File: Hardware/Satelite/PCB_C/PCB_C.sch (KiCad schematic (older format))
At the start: 54 parts, among them IC1 MCP1501T-33E_CHY, IC3 BQ24392RSER, J1 Conn_01x06, J3 Conector_PCB_B-C, J4 Conector_Expansion_CanSat, J5 USB_B_Micro, J6 Conn_02x03_Counter_Clockwise, M1 Spacer, M2 Spacer, M3 Spacer, U1 NTB0104BQ,115, U2 TCA9802DGKR, U3 ESP32-WROOM-32, U4 NTB0104BQ,115, U7 PIC16LF18325-ISL, Y1 LFXTAL016178

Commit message: Agregadas librerías a PCB_C y renombrados pines no usado en el conector B-C
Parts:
- removed U3: ESP32-WROOM-32, RF_Module:ESP32-WROOM-32, symbol PCB_C-rescue:ESP32-WROOM-32-RF_Module
- added U?: ESP32-WROOM-32, RF_Module:ESP32-WROOM-32, symbol RF_Module:ESP32-WROOM-32
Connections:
- net labels removed: ISET
- wire segments 305 -> 303
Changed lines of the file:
@@
 EESchema Schematic File Version 4
 LIBS:PCB_C-cache
-EELAYER 26 0
+EELAYER 29 0
 EELAYER END
 $Descr A3 16535 11693
@@
 Text Label 15100 2200 0    50   ~ 0
 GPOUT
-Text Label 15100 1700 0    50   ~ 0
-ISET
 Text Label 15100 1800 0    50   ~ 0
 CHG
@@
 Wire Wire Line
 	15000 2100 15400 2100
-Wire Wire Line
-	15000 1700 15400 1700
 Wire Wire Line
 	15000 1800 15400 1800
@@
 Text Label 5400 1950 0    50   ~ 0
 CHG
-Text Label 7900 2150 2    50   ~ 0
-ISET
 Text Label 7900 2250 2    50   ~ 0
 SDO
@@
 	10250 2200 10250 2300
 Connection ~ 10100 2200
-Wire Wire Line
-	7250 2150 7900 2150
 $Comp
 L power:GND #PWR047
@@
 Wire Wire Line
 	8150 7350 7750 7350
-$Comp
-L PCB_C-rescue:ESP32-WROOM-32-RF_Module U3
-U 1 1 5D74DFF0
-P 6650 2850
-F 0 "U3" H 5900 4350 50  0000 C CNN
-F 1 "ESP32-WROOM-32" H 6200 4250 50  0000 C CNN
-F 2 "RF_Module:ESP32-WROOM-32" H 6650 1350 50  0001 C CNN
-F 3 "https://www.espressif.com/sites/default/files/documentation/esp32-wroom-32_datasheet_en.pdf" H 6350 2900 50  0001 C CNN
-F 4 "ESP32-WROOM-32" H 6650 2850 50  0001 C CNN "Manufacturer Part Number"
-	1    6650 2850
-	1    0    0    -1
-$EndComp
 $Comp
 L power:GND #PWR017
@@
 EndData
 $EndBitmap
+$Comp
+L RF_Module:ESP32-WROOM-32 U?
+U 1 1 5D11D3F2
+P 6650 2850
+F 0 "U?" H 7050 4350 50  0000 C CNN
+F 1 "ESP32-WROOM-32" H 7050 4250 50  0000 C CNN
+F 2 "RF_Module:ESP32-WROOM-32" H 6650 1350 50  0001 C CNN
+F 3 "https://www.espressif.com/sites/default/files/documentation/esp32-wroom-32_datasheet_en.pdf" H 6350 2900 50  0001 C CNN
+	1    6650 2850
+	1    0    0    -1
+$EndComp
 $EndSCHEMATC

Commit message: Eliminado circuito de detección de cargador de PCB_C, siempre usamos toda la corriente de carga ahora.
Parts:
- removed IC3: BQ24392RSER, SamacSys_Parts:RSE(R-PUQFN-N10), symbol SamacSys_Parts:BQ24392RSER
- removed R8: 5k6, Resistor_SMD:R_0603_1608Metric_Pad1.05x0.95mm_HandSolder, symbol Device:R
- removed R9: 10k, Resistor_SMD:R_0603_1608Metric_Pad1.05x0.95mm_HandSolder, symbol Device:R
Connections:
- wire segments 303 -> 286
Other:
- note added: "USB"
- note removed: "USB y detección de cargador"
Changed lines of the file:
@@
 $EndComp
-Wire Wire Line
-	15350 9100 14800 9100
-Wire Wire Line
-	14800 9000 15350 9000
 Wire Wire Line
 	15650 9400 15650 9450
@@
 Wire Wire Line
 	15750 9450 15700 9450
-$Comp
-L SamacSys_Parts:BQ24392RSER IC3
-U 1 1 5BBE8A84
-P 13300 8800
-F 0 "IC3" H 14050 9065 50  0000 C CNN
-F 1 "BQ24392RSER" H 14050 8974 50  0000 C CNN
-F 2 "SamacSys_Parts:RSE(R-PUQFN-N10)" H 14650 8900 50  0001 L CNN
-F 3 "http://www.ti.com/lit/gpn/bq24392" H 14650 8800 50  0001 L CNN
-F 4 "SPST USB 2.0 High-Speed Switch With Battery Charging Detection" H 14650 8700 50  0001 L CNN "Description"
-F 5 "Texas Instruments" H 14650 8500 50  0001 L CNN "Manufacturer_Name"
-F 6 "BQ24392RSER" H 14650 8400 50  0001 L CNN "Manufacturer Part Number"
-F 7 "8279327P" H 14650 8300 50  0001 L CNN "RS Part Number"
-F 8 "http://uk.rs-online.com/web/p/products/8279327P" H 14650 8200 50  0001 L CNN "RS Price/Stock"
-F 9 "BQ24392RSER" H 14650 8100 50  0001 L CNN "Arrow Part Number"
-F 10 "https://www.arrow.com/en/products/bq24392rser/texas-instruments" H 14650 8000 50  0001 L CNN "Arrow Price/Stock"
-	1    13300 8800
-	1    0    0    -1
-$EndComp
-Wire Wire Line
-	14800 8800 15050 8800
 Wire Wire Line
 	15050 8750 15050 8800
-Connection ~ 15050 8800
 Wire Wire Line
 	15050 8800 15350 8800
-$Comp
-L power:GND #PWR058
-U 1 1 5BBEBEBA
-P 14950 9500
-F 0 "#PWR058" H 14950 9250 50  0001 C CNN
-F 1 "GND" H 14955 9327 50  0000 C CNN
-F 2 "" H 14950 9500 50  0001 C CNN
-F 3 "" H 14950 9500 50  0001 C CNN
-	1    14950 9500
-	1    0    0    -1
-$EndComp
-Wire Wire Line
-	14800 9300 14950 9300
-Wire Wire Line
-	14950 9300 14950 9500
-Text Label 11900 9050 0    50   ~ 0
-CHG_DETECT
-$Comp
-L power:VBUS #PWR045
-U 1 1 5BC0A264
-P 13050 9250
-F 0 "#PWR045" H 13050 9100 50  0001 C CNN
-F 1 "VBUS" H 13065 9423 50  0000 C CNN
-F 2 "" H 13050 9250 50  0001 C CNN
-F 3 "" H 13050 9250 50  0001 C CNN
-	1    13050 9250
-	1    0    0    -1
-$EndComp
-Wire Notes Line
-	11800 8100 16000 8100
+Wire Notes Line
+	14850 8100 16000 8100
 Wire Notes Line
 	16000 8100 16000 9800
 Wire Notes Line
-	16000 9800 11800 9800
-Wire Notes Line
-	11800 9800 11800 8100
-Text Notes 12550 8350 0    118  ~ 0
-USB y detección de cargador
+	16000 9800 14850 9800
+Wire Notes Line
+	14850 9800 14850 8100
+Text Notes 15200 8350 0    118  ~ 0
+USB
 Wire Notes Line
 	550  3050 3550 3050
@@
 Text Label 5250 5800 0    50   ~ 0
 I_SENSE_BATT
-Text Label 5400 1850 0    50   ~ 0
-CHG_DETECT
 Text Label 7900 2050 2    50   ~ 0
 AUX_ENABLE
@@
 	5900 5800 5250 5800
 Wire Wire Line
-	5400 1850 6050 1850
-Wire Wire Line
 	7900 3250 7250 3250
 Wire Wire Line
@@
 	15100 4650 15550 4650
 $Comp
-L Device:R R8
-U 1 1 5C2BF325
-P 12600 8850
-F 0 "R8" H 12670 8896 50  0000 L CNN
-F 1 "5k6" H 12670 8804 50  0000 L CNN
-F 2 "Resistor_SMD:R_0603_1608Metric_Pad1.05x0.95mm_HandSolder" V 12530 8850 50  0001 C CNN
-F 3 "~" H 12600 8850 50  0001 C CNN
-F 4 "RC0603FR-075K6L" H 12600 8850 50  0001 C CNN "Manufacturer Part Number"
-	1    12600 8850
-	1    0    0    -1
-$EndComp
-Wire Wire Line
-	13050 9250 13250 9250
-Wire Wire Line
-	13250 9250 13250 9200
-Wire Wire Line
-	13250 9200 13300 9200
-$Comp
-L Device:R R9
-U 1 1 5C3B0D3B
-P 12600 9250
-F 0 "R9" H 12670 9296 50  0000 L CNN
-F 1 "10k" H 12670 9204 50  0000 L CNN
-F 2 "Resistor_SMD:R_0603_1608Metric_Pad1.05x0.95mm_HandSolder" V 12530 9250 50  0001 C CNN
-F 3 "~" H 12600 9250 50  0001 C CNN
-F 4 "RC0603JR-0710KL" H 12600 9250 50  0001 C CNN "Manufacturer Part Number"
-	1    12600 9250
-	1    0    0    -1
-$EndComp
-Wire Wire Line
-	13300 9000 13050 9000
-Wire Wire Line
-	13050 9000 13050 8650
-Wire Wire Line
-	13050 8650 12600 8650
-$Comp
-L power:GND #PWR011
-U 1 1 5C412A14
-P 12600 9500
-F 0 "#PWR011" H 12600 9250 50  0001 C CNN
-F 1 "GND" H 12605 9327 50  0000 C CNN
-F 2 "" H 12600 9500 50  0001 C CNN
-F 3 "" H 12600 9500 50  0001 C CNN
-	1    12600 9500
-	1    0    0    -1
-$EndComp
-Wire Wire Line
-	12600 9400 12600 9500
-Wire Wire Line
-	12600 9000 12600 9050
-Wire Wire Line
-	12600 8650 12600 8700
-Wire Wire Line
-	12600 9100 12600 9050
-Connection ~ 12600 9050
-$Comp
 L power:+BATT #PWR01
 U 1 1 5BC3E6F0
@@
 	-1   0    0    -1
 $EndComp
-Wire Wire Line
-	11900 9050 12600 9050
 $Comp
 L Graphic:Logo_Open_Hardware_Large #LOGO1

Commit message: Nuevo conector entre PCB_B y PCB_C, más fácil de soldar y robusto
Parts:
- J3: Manufacturer Part Number 10132797-025100LF -> 53307-2071; Notes Hecho con dos 10132797-025100LF y sus dos opuestos 10132798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 -> Hecho con dos 53307-2071 y sus dos opuestos 52465-2071
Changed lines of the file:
@@
 F 2 "AXTEC:Conector_PCB_B-C_Lado_C" H 14150 2200 50  0001 C CNN
 F 3 "" H 14150 2200 50  0001 C CNN
-F 4 "Hecho con dos 10132797-025100LF y sus dos opuestos 10132798-022100LF" H 0   -150 50  0001 C CNN "Notes"
-F 5 "10132797-025100LF" H 14250 1450 50  0001 C CNN "Manufacturer Part Number"
+F 4 "Hecho con dos 53307-2071 y sus dos opuestos 52465-2071" H 0   -150 50  0001 C CNN "Notes"
+F 5 "53307-2071" H 14250 1450 50  0001 C CNN "Manufacturer Part Number"
 F 6 "2" H 14250 1450 50  0001 C CNN "Quantity"
 	1    14250 1450

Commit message: ESP32 tamaño compacto sin antena PCB
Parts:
- removed U?: ESP32-WROOM-32, RF_Module:ESP32-WROOM-32, symbol RF_Module:ESP32-WROOM-32
- added U?: ESP32-WROOM-32U, RF_Module:ESP32-WROOM-32U, symbol RF_Module:ESP32-WROOM-32U
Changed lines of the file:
@@
 $EndBitmap
 $Comp
-L RF_Module:ESP32-WROOM-32 U?
-U 1 1 5D11D3F2
+L RF_Module:ESP32-WROOM-32U U?
+U 1 1 5CCE43C3
 P 6650 2850
 F 0 "U?" H 7050 4350 50  0000 C CNN
-F 1 "ESP32-WROOM-32" H 7050 4250 50  0000 C CNN
-F 2 "RF_Module:ESP32-WROOM-32" H 6650 1350 50  0001 C CNN
-F 3 "https://www.espressif.com/sites/default/files/documentation/esp32-wroom-32_datasheet_en.pdf" H 6350 2900 50  0001 C CNN
+F 1 "ESP32-WROOM-32U" H 7050 4250 50  0000 C CNN
+F 2 "RF_Module:ESP32-WROOM-32U" H 6650 1350 50  0001 C CNN
+F 3 "https://www.espressif.com/sites/default/files/documentation/esp32-wroom-32d_esp32-wroom-32u_datasheet_en.pdf" H 6350 2900 50  0001 C CNN
+F 4 "ESP32-WROOM-32U" H 6650 2850 50  0001 C CNN "Manufacturer Part Number"
 	1    6650 2850
 	1    0    0    -1

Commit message: Agregado conversor USB-Serie en PCB_C para poder programar el ESP32 desde USB
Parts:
- removed J1: Conn_01x06, Connector_PinHeader_2.54mm:PinHeader_1x06_P2.54mm_Vertical, symbol Connector_Generic:Conn_01x06
- removed JP1: BOM_Jumper, AXTEC:Empty_Footprint, symbol AXTEC_IC:BOM_Jumper
- removed L1: Inductor, Inductor_SMD:L_0805_2012Metric_Pad1.15x1.40mm_HandSolder, symbol Device:L_Core_Iron
- added C10: 100nF, Capacitor_SMD:C_0402_1005Metric, symbol Device:C_Small
- added C6: 4.7uF, Capacitor_SMD:C_0805_2012Metric_Pad1.15x1.40mm_HandSolder, symbol Device:C_Small
- added C7, C8: 47pF, Capacitor_SMD:C_0402_1005Metric, symbol Device:C_Small
- added JP1: Jumper_2_Bridged, Jumper:SolderJumper-2_P1.3mm_Bridged_Pad1.0x1.5mm, symbol Jumper:Jumper_2_Bridged
- added R8: 27R, Resistor_SMD:R_0603_1608Metric_Pad1.05x0.95mm_HandSolder, symbol Device:R
- added R9: 100k, Resistor_SMD:R_0603_1608Metric_Pad1.05x0.95mm_HandSolder, symbol Device:R
- added U3: FT231XQ, Package_DFN_QFN:QFN-20-1EP_4x4mm_P0.5mm_EP2.5x2.5mm, symbol Interface_USB:FT231XQ
- R6: value 100k -> 27R; Manufacturer Part Number RC0603JR-07100KL -> RC0603FR-0727RL
- gave numbers to parts that had none: 1
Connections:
- net labels added: D+, D-
- wire segments 286 -> 301
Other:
- note removed: "Header programación"
- moved on the sheet: C1, C13, C16, IC1, J5, M1, M2, M3, MH1, R7, TP1, TP10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

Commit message: Cambio de MCU de ESP32 a nRF52840
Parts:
- removed C13, C16: 1uF, Capacitor_SMD:C_0402_1005Metric, symbol Device:C_Small
- removed J6: Conn_02x03_Counter_Clockwise, Connector_PinHeader_1.27mm:PinHeader_2x03_P1.27mm_Vertical_SMD, symbol Connector_Generic:Conn_02x03_Counter_Clockwise
- removed JP1: Jumper_2_Bridged, Jumper:SolderJumper-2_P1.3mm_Bridged_Pad1.0x1.5mm, symbol Jumper:Jumper_2_Bridged
- removed R2, R3: 10k, Resistor_SMD:R_0603_1608Metric_Pad1.05x0.95mm_HandSolder, symbol Device:R
- removed R5, R7, R9: 100k, Resistor_SMD:R_0603_1608Metric_Pad1.05x0.95mm_HandSolder, symbol Device:R
- removed U3: FT231XQ, Package_DFN_QFN:QFN-20-1EP_4x4mm_P0.5mm_EP2.5x2.5mm, symbol Interface_USB:FT231XQ
- removed U5: ESP32-WROOM-32U, RF_Module:ESP32-WROOM-32U, symbol RF_Module:ESP32-WROOM-32U
- removed U7: PIC16LF18325-ISL, Package_SO:SOIC-14_3.9x8.7mm_P1.27mm, symbol MCU_Microchip_PIC16:PIC16LF18325-ISL
- added U3: W25Q32JVSSIQ, Package_SO:SOIC-8_3.9x4.9mm_P1.27mm, symbol SamacSys_Parts:W25Q32BVSSIG
- added U5: BL654, SamacSys_Parts:45100001, symbol AXTEC_IC:BL654
- C10: value 100nF -> 1uF; Manufacturer Part Number GCM155R71C104KA55D -> GRM155R61E105KA12D
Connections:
- net labels added: EXT_IO2, EXT_IO3, MCLK, MCS, MMISO, MMOSI, SWCLK, SWDIO, SWO, nRST
- net labels removed: EN, GPIO0, ICSDAT, ICSPCLK, MCLR
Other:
- note added: "SLOW"
- moved on the sheet: C3, C4, C6, C7, C8, J5, R1, R4, R6, R8, Y1

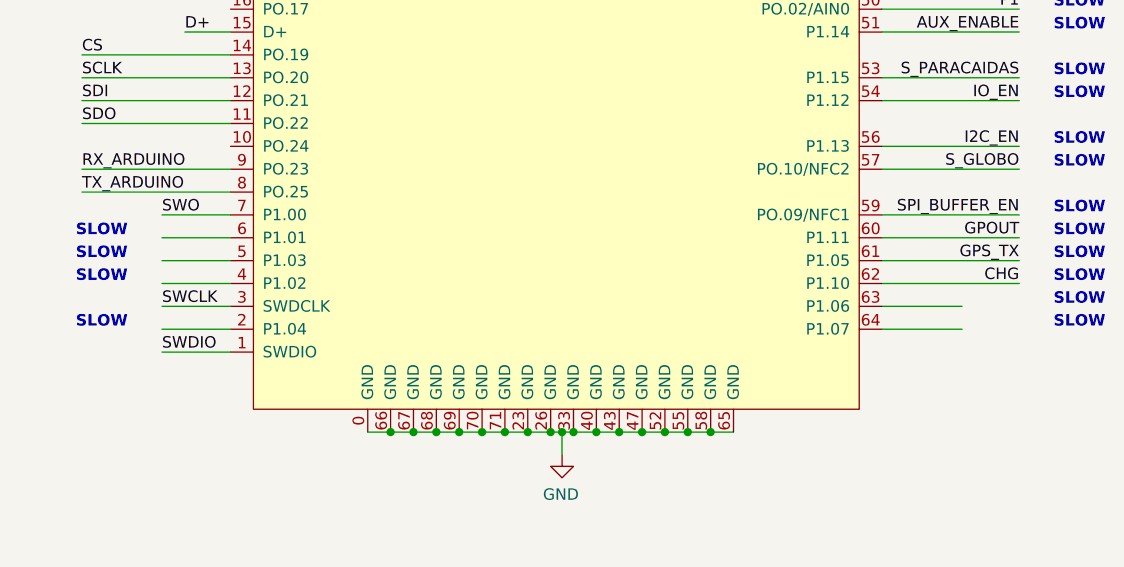
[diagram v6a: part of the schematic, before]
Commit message: Eliminación de wires no usadas en esquema de PCB_C
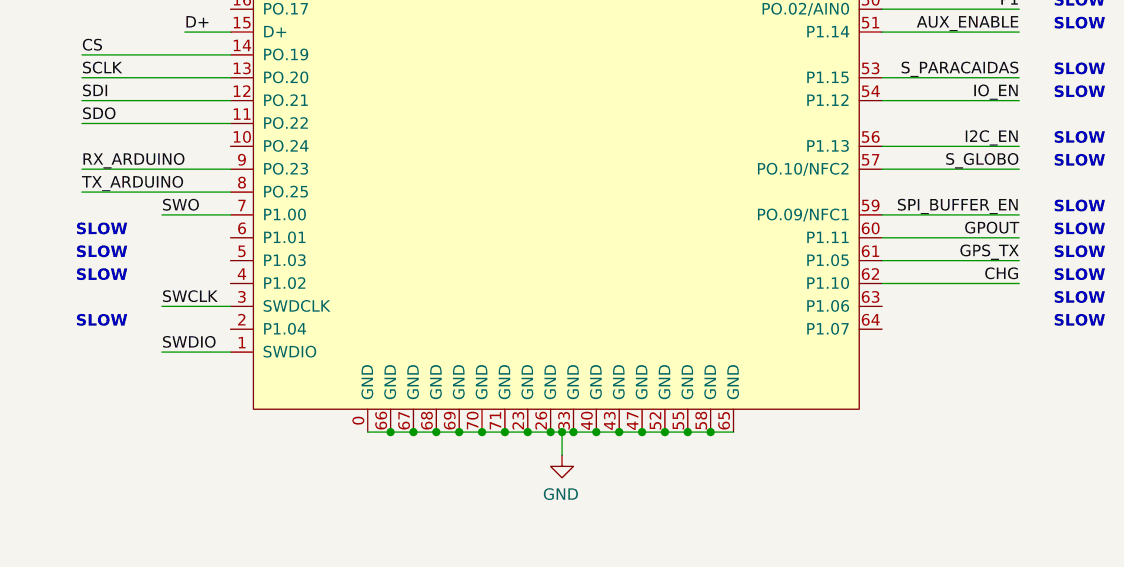
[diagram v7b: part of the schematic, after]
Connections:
- wire segments 301 -> 295
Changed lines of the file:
@@
 	9650 5050 10250 5050
 Wire Wire Line
-	9650 5550 10000 5550
-Wire Wire Line
-	9650 5450 10000 5450
-Wire Wire Line
 	9650 5250 10250 5250
-Wire Wire Line
-	6800 5550 6500 5550
-Wire Wire Line
-	6800 5350 6500 5350
-Wire Wire Line
-	6500 5250 6800 5250
-Wire Wire Line
-	6800 5150 6500 5150
 $Comp
 L power:GND #PWR015

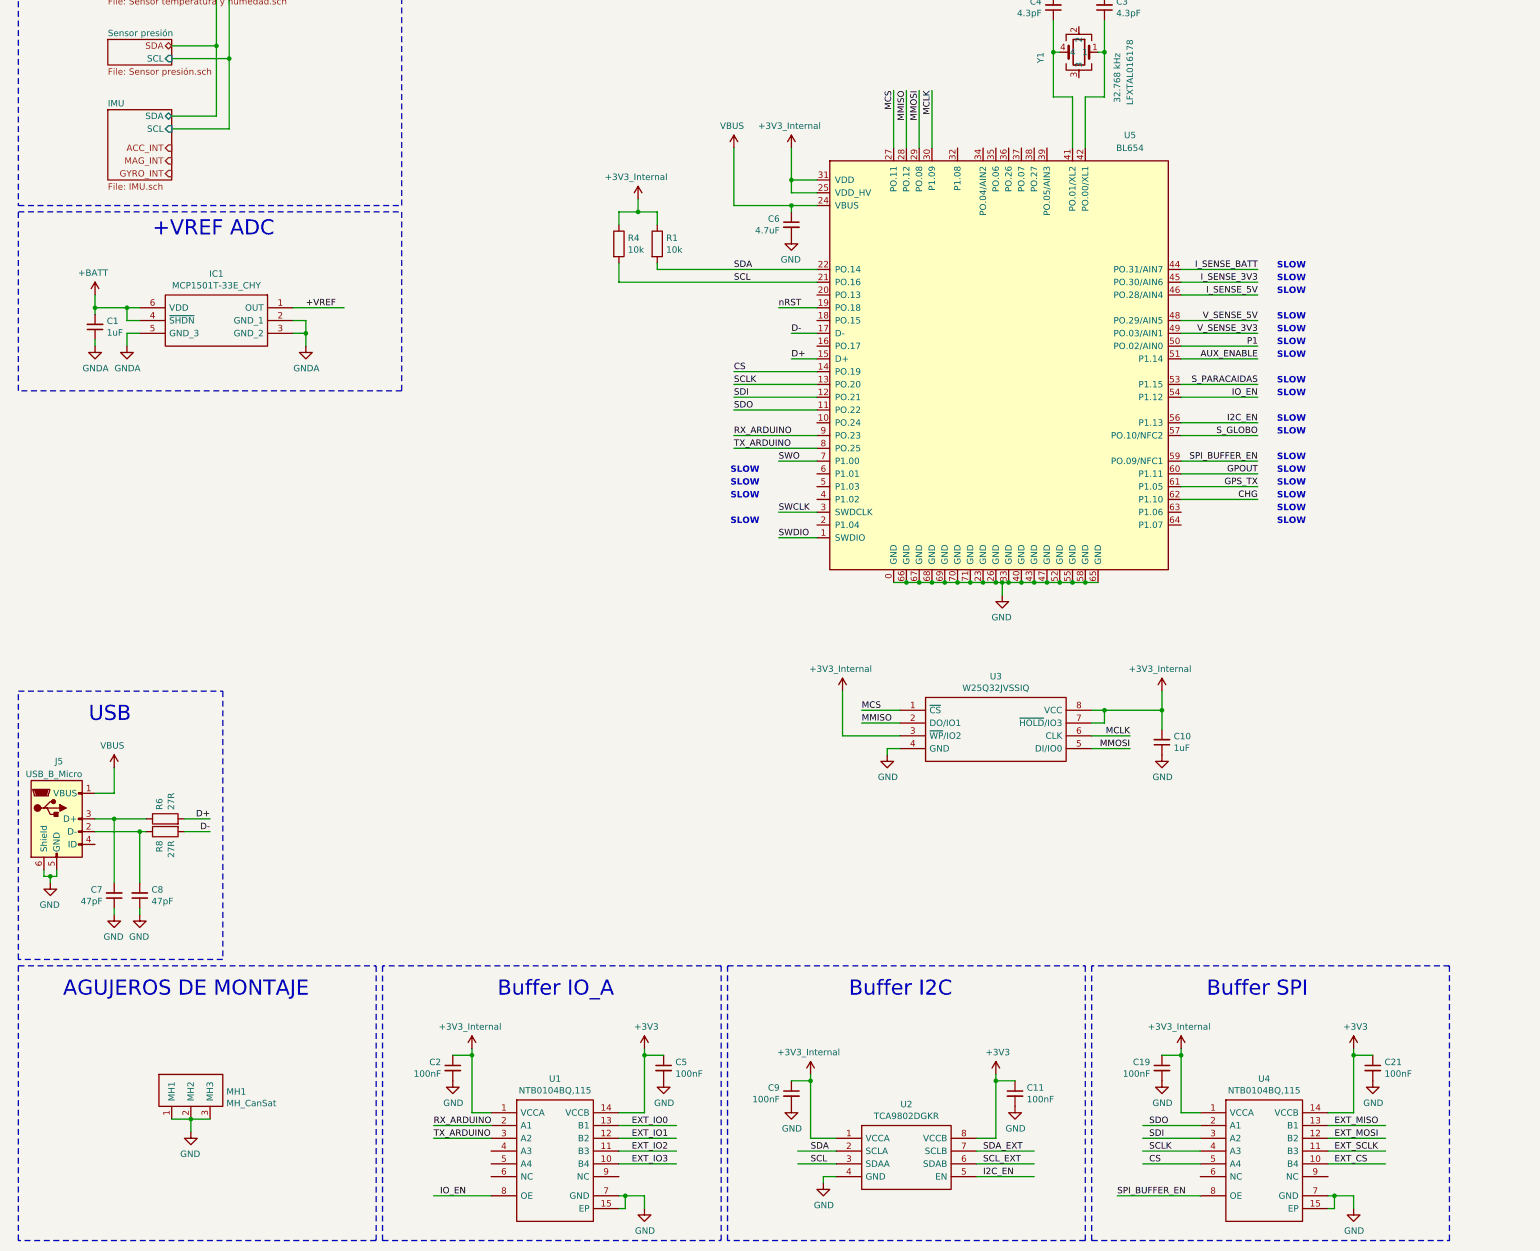
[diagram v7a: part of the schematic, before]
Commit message: Nuevos buffers bidireccionales en PCB_C. Deberían solucionar los problemas que existían con los antiguos buffers que eran muy sensibles a cualquier carga que se colocara (analizador lógico por ejemplo)
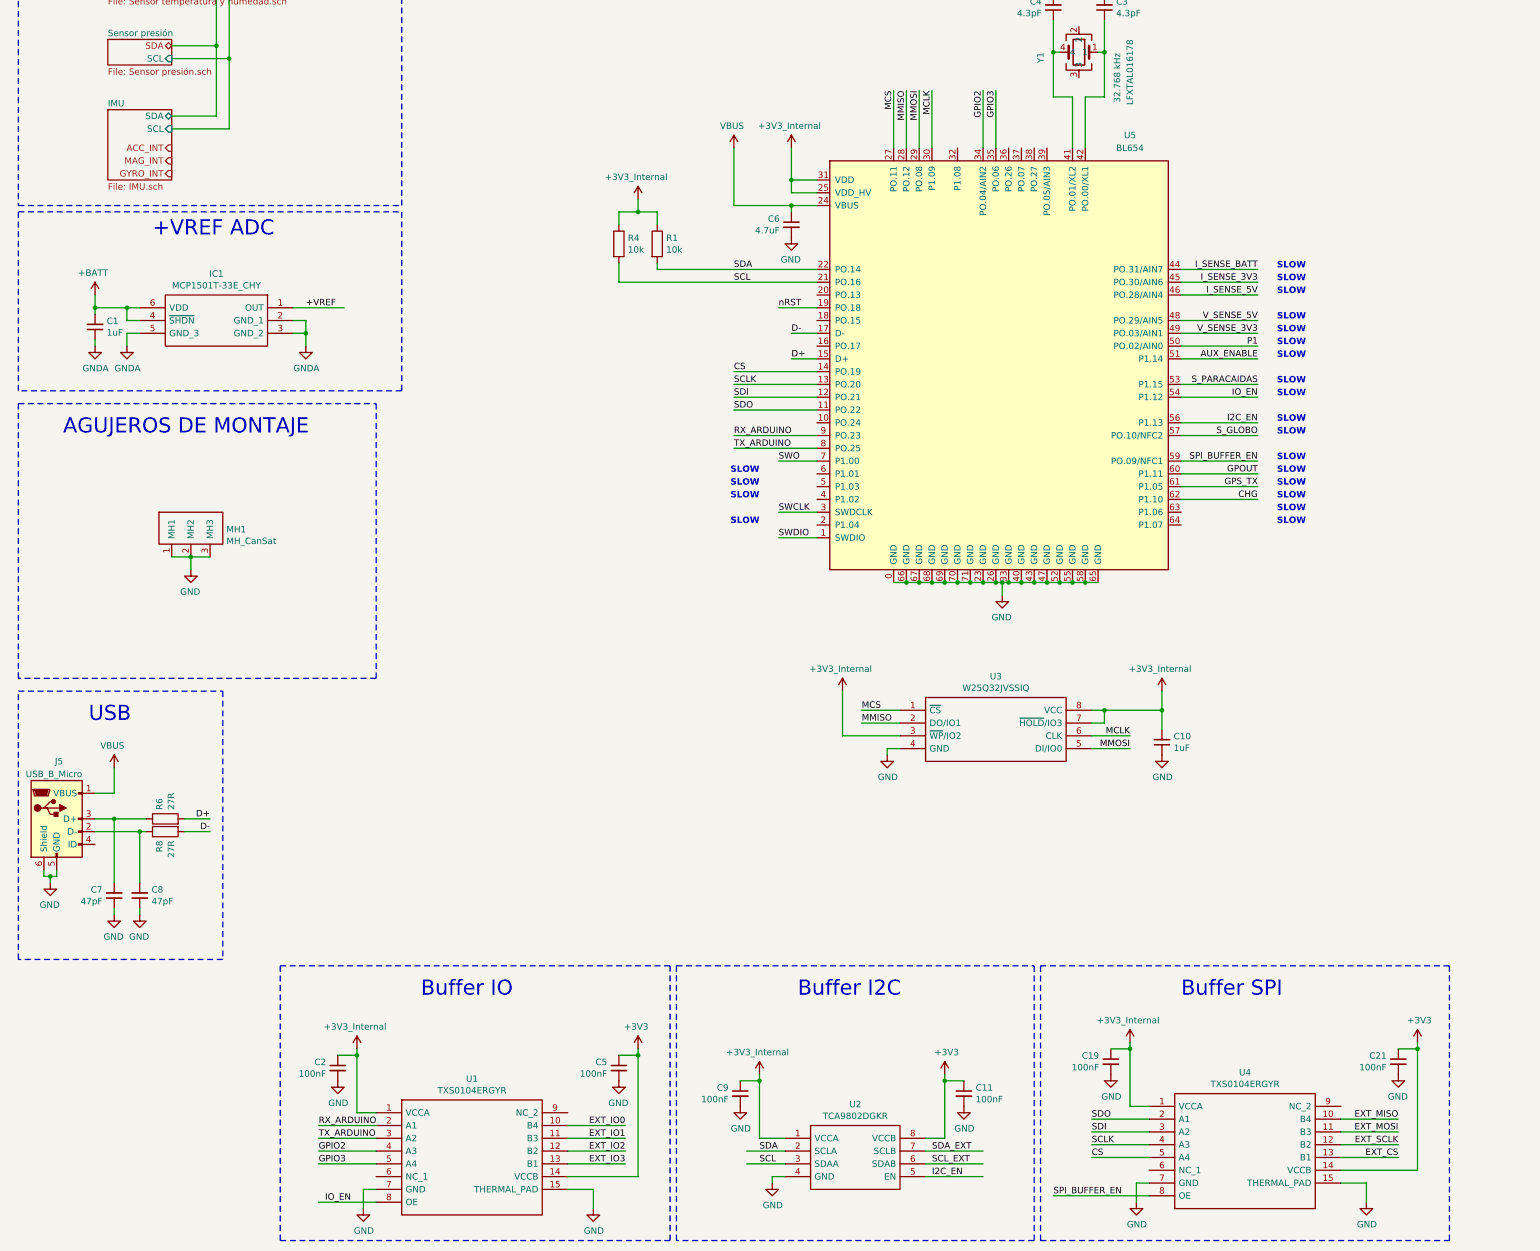
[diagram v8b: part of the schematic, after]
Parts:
- removed U1, U4: NTB0104BQ,115, SamacSys_Parts:NTB0104BQ115, symbol SamacSys_Parts:NTB0104BQ,115
- added U1, U4: TXS0104ERGYR, RGY(S-PVQFN-N14), symbol SamacSys_Parts:TXS0104ERGYR
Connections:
- net labels added: GPIO2, GPIO3
- wire segments 295 -> 297
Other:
- note added: "Buffer IO"
- note removed: "Buffer IO_A"
- moved on the sheet: C11, C19, C2, C21, C5, C9, MH1, U2
